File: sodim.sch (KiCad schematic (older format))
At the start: 4 parts

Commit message: Update edge connector
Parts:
- J? (x2): footprint lpddr4-testbed-footprints:SODIMM_DDR4_EDGE -> antmicro-footprints:SODIMM_DDR4_EDGE; symbol lpddr4-testbed:ddr4-sodimm-edge-connector -> antmicroMemoryConnectorsPCCardSockets:ddr4-sodimm-edge-connector
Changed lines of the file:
@@
 SODIMM Connector
 $Comp
-L lpddr4-testbed:ddr4-sodimm-edge-connector J?
+L antmicroMemoryConnectorsPCCardSockets:ddr4-sodimm-edge-connector J?
 U 2 1 5FF3EE7F
 P 10650 5525
@@
 F 0 "J?" H 10650 8992 50  0000 C CNN
 F 1 "ddr4-sodimm-edge-connector" H 10650 8901 50  0000 C CNN
-F 2 "lpddr4-testbed-footprints:SODIMM_DDR4_EDGE" H 10350 1925 50  0001 L BNN
+F 2 "antmicro-footprints:SODIMM_DDR4_EDGE" H 10350 1925 50  0001 L BNN
 F 3 "" H 11650 5625 50  0001 L BNN
 	2    10650 5525
@@
 $EndComp
 $Comp
-L lpddr4-testbed:ddr4-sodimm-edge-connector J?
+L antmicroMemoryConnectorsPCCardSockets:ddr4-sodimm-edge-connector J?
 U 1 1 5FF3EE85
 P 6525 5800
@@
 F 0 "J?" H 6525 9365 50  0000 C CNN
 F 1 "ddr4-sodimm-edge-connector" H 6525 9274 50  0000 C CNN
-F 2 "lpddr4-testbed-footprints:SODIMM_DDR4_EDGE" H 6225 2200 50  0001 L BNN
+F 2 "antmicro-footprints:SODIMM_DDR4_EDGE" H 6225 2200 50  0001 L BNN
 F 3 "" H 7525 5900 50  0001 L BNN
 	1    6525 5800

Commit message: Connect power supplies and CHANNEL A signals to edge connector
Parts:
- removed C?: C_100n_0402_6V3, lpddr4-testbed-footprints:0402-cap, symbol lpddr4-testbed:C_100n_0402_6V3
- removed J? (x2): ddr4-sodimm-edge-connector, antmicro-footprints:SODIMM_DDR4_EDGE, symbol antmicroMemoryConnectorsPCCardSockets:ddr4-sodimm-edge-connector
- removed R?: R_40R2_0402, lpddr4-testbed-footprints:0402-res, symbol lpddr4-testbed:R_40R2_0402
- added J1: ddr4-sodimm-edge-connector, antmicro-footprints:SODIMM_DDR4_EDGE, symbol antmicroMemoryConnectorsPCCardSockets:ddr4-sodimm-edge-connector
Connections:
- net labels added: CA_0A, CA_1A, CKE0_A, CK_CA, CK_TA, CS0_A, DMI_0A, DMI_1A, DQ00_A, DQ01_A, DQ02_A, DQ03_A, DQ04_A, DQ05_A, DQ06_A, DQ07_A, DQ08_A, DQ09_A, DQ10_A, DQ11_A, DQ12_A, DQ13_A, DQ14_A, DQ15_A, DQ_S0_CA, DQ_S0_TA, DQ_S1_CA, DQ_S1_TA, VDD1, VDD2, VDDQ
- net labels removed: ACT_N, ALERT_N, BA0, BA1, BG0, BG1, CA0_A, CA0_B, CA1_A, CA1_B, CA2_B, CA3_B, CA4_B, CA5_B, CK0_C, CK0_T, CK1_C, CK1_T, CKE_0, CKE_1, CS0_N, CS_1_N, DDRVCC, DM0_N, DM1_N, DM2_N, DM3_N, DQ00, DQ01, DQ02, DQ03, DQ04, DQ05, DQ06, DQ07, DQ08, DQ09, DQ10, DQ11, DQ12, DQ13, DQ14, DQ15, DQ16, DQ17, DQ18, DQ19, DQ20, DQ21, DQ22, DQ23, DQ24, DQ25, DQ26, DQ27, DQ28, DQ29, DQ30, DQ31, DQS0_C, DQS0_T, DQS1_C, DQS1_T, DQS2_C, DQS2_T, DQS3_C, DQS3_T, EVENT_N, ODT0, ODT1, PARITY, RESET_CONN_N, SA0, SA1, SCL, SDA, VDDSPD, VPP, VREFCA, VTT
- wire segments 321 -> 214
- no-connect marks 65 -> 0
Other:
- note added: "1V1_SYS"
- note added: "1V8_SYS"
- note added: "VDDQ"
- note removed: "Bank adress"
- note removed: "Bank group\n"
- note removed: "Second LPDDR4 die"
- note removed: "Single LPDDR4 die"
- note removed: "What is taht pin?"

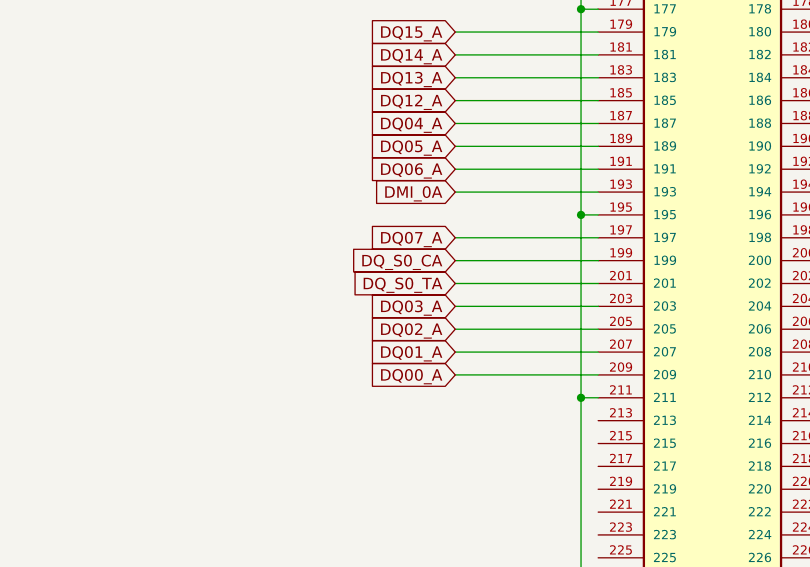
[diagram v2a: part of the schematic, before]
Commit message: Reverse connections of DQ4_A ... DQ0_A
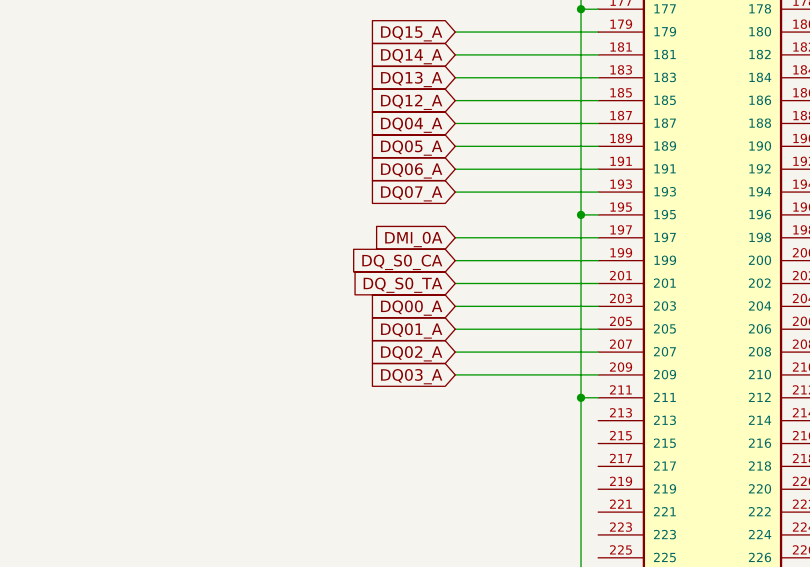
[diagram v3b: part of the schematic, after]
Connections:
- net DMI_0A: now also J1.197; no longer J1.193
- net DQ00_A: now also J1.203; no longer J1.209
- net DQ01_A: now also J1.205; no longer J1.207
- net DQ02_A: now also J1.207; no longer J1.205
- net DQ03_A: now also J1.209; no longer J1.203
- net DQ07_A: now also J1.193; no longer J1.197
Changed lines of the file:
@@
 Wire Wire Line
 	9500 5700 8875 5700
+Text GLabel 8875 5900 0    50   Input ~ 0
+DMI_0A
+Wire Wire Line
+	9500 5900 8875 5900
 Text GLabel 8875 5700 0    50   Input ~ 0
-DMI_0A
-Wire Wire Line
-	9500 5900 8875 5900
-Text GLabel 8875 5900 0    50   Input ~ 0
 DQ07_A
 Wire Wire Line
@@
 Wire Wire Line
 	9500 6200 8875 6200
+Text GLabel 8875 6500 0    50   Input ~ 0
+DQ03_A
+Wire Wire Line
+	9500 6300 8875 6300
+Text GLabel 8875 6400 0    50   Input ~ 0
+DQ02_A
+Wire Wire Line
+	9500 6400 8875 6400
+Text GLabel 8875 6300 0    50   Input ~ 0
+DQ01_A
+Wire Wire Line
+	9500 6500 8875 6500
 Text GLabel 8875 6200 0    50   Input ~ 0
-DQ03_A
-Wire Wire Line
-	9500 6300 8875 6300
-Text GLabel 8875 6300 0    50   Input ~ 0
-DQ02_A
-Wire Wire Line
-	9500 6400 8875 6400
-Text GLabel 8875 6400 0    50   Input ~ 0
-DQ01_A
-Wire Wire Line
-	9500 6500 8875 6500
-Text GLabel 8875 6500 0    50   Input ~ 0
 DQ00_A
 Wire Wire Line
@@
 	5725 2500 5850 2500
 $Comp
-L lpddr4-testbed:GND #PWR?
+L lpddr4-testbed:GND #PWR0101
 U 1 1 600CF473
 P 5850 9125
-F 0 "#PWR?" H 5850 8875 50  0001 C CNN
+F 0 "#PWR0101" H 5850 8875 50  0001 C CNN
 F 1 "GND" H 5855 8952 50  0000 C CNN
 F 2 "" H 5850 9125 50  0001 C CNN
@@
 $EndComp
 $Comp
-L lpddr4-testbed:GND #PWR?
+L lpddr4-testbed:GND #PWR0102
 U 1 1 600CF7AC
 P 9425 9125
-F 0 "#PWR?" H 9425 8875 50  0001 C CNN
+F 0 "#PWR0102" H 9425 8875 50  0001 C CNN
 F 1 "GND" H 9430 8952 50  0000 C CNN
 F 2 "" H 9425 9125 50  0001 C CNN
@@
 	4600 2500 4600 2600
 $Comp
-L lpddr4-testbed:GND #PWR?
+L lpddr4-testbed:GND #PWR0103
 U 1 1 600F8128
 P 4600 9125
-F 0 "#PWR?" H 4600 8875 50  0001 C CNN
+F 0 "#PWR0103" H 4600 8875 50  0001 C CNN
 F 1 "GND" H 4605 8952 50  0000 C CNN
 F 2 "" H 4600 9125 50  0001 C CNN
@@
 	10550 3700 10550 4400
 $Comp
-L lpddr4-testbed:GND #PWR?
+L lpddr4-testbed:GND #PWR0104
 U 1 1 6032AE1D
 P 10550 9125
-F 0 "#PWR?" H 10550 8875 50  0001 C CNN
+F 0 "#PWR0104" H 10550 8875 50  0001 C CNN
 F 1 "GND" H 10555 8952 50  0000 C CNN
 F 2 "" H 10550 9125 50  0001 C CNN

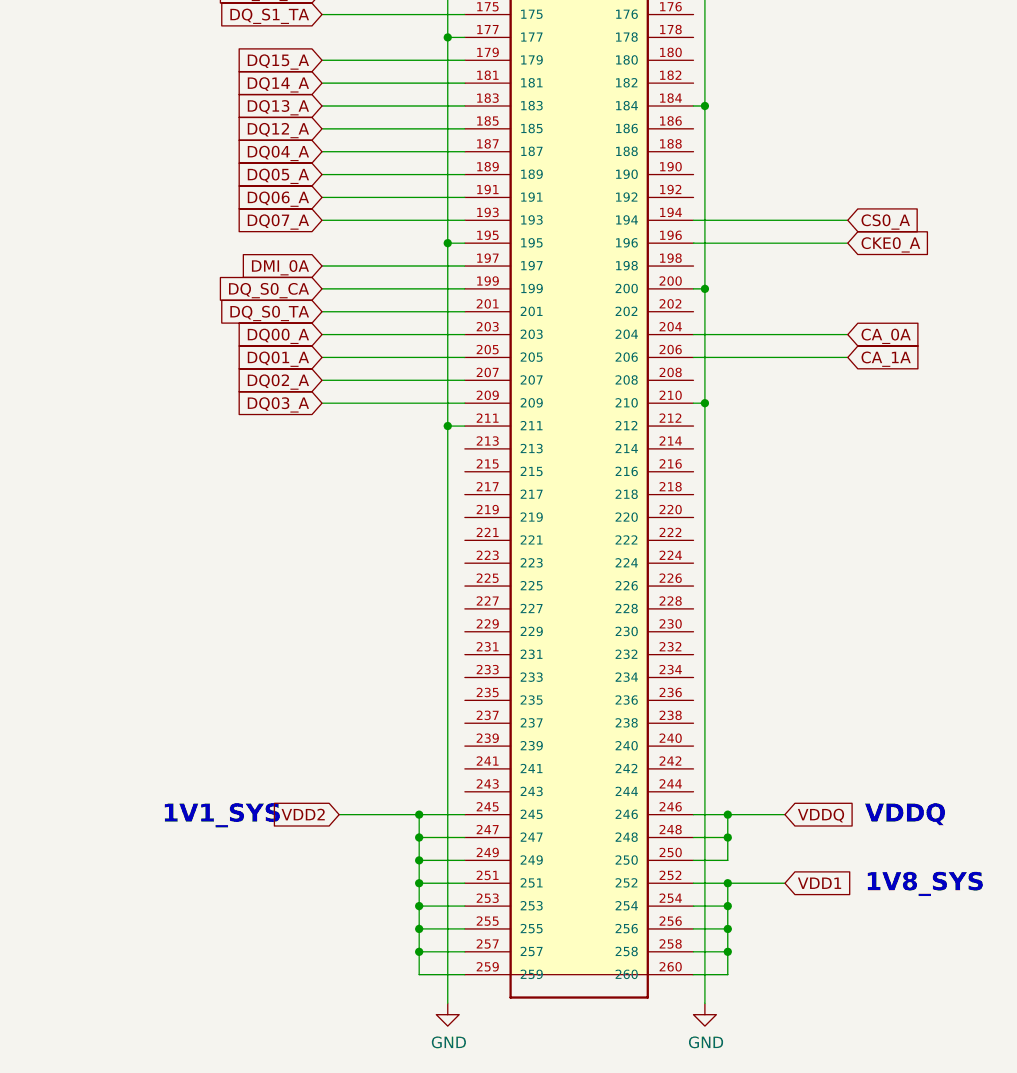
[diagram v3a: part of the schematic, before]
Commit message: Fully routed, DRC clean
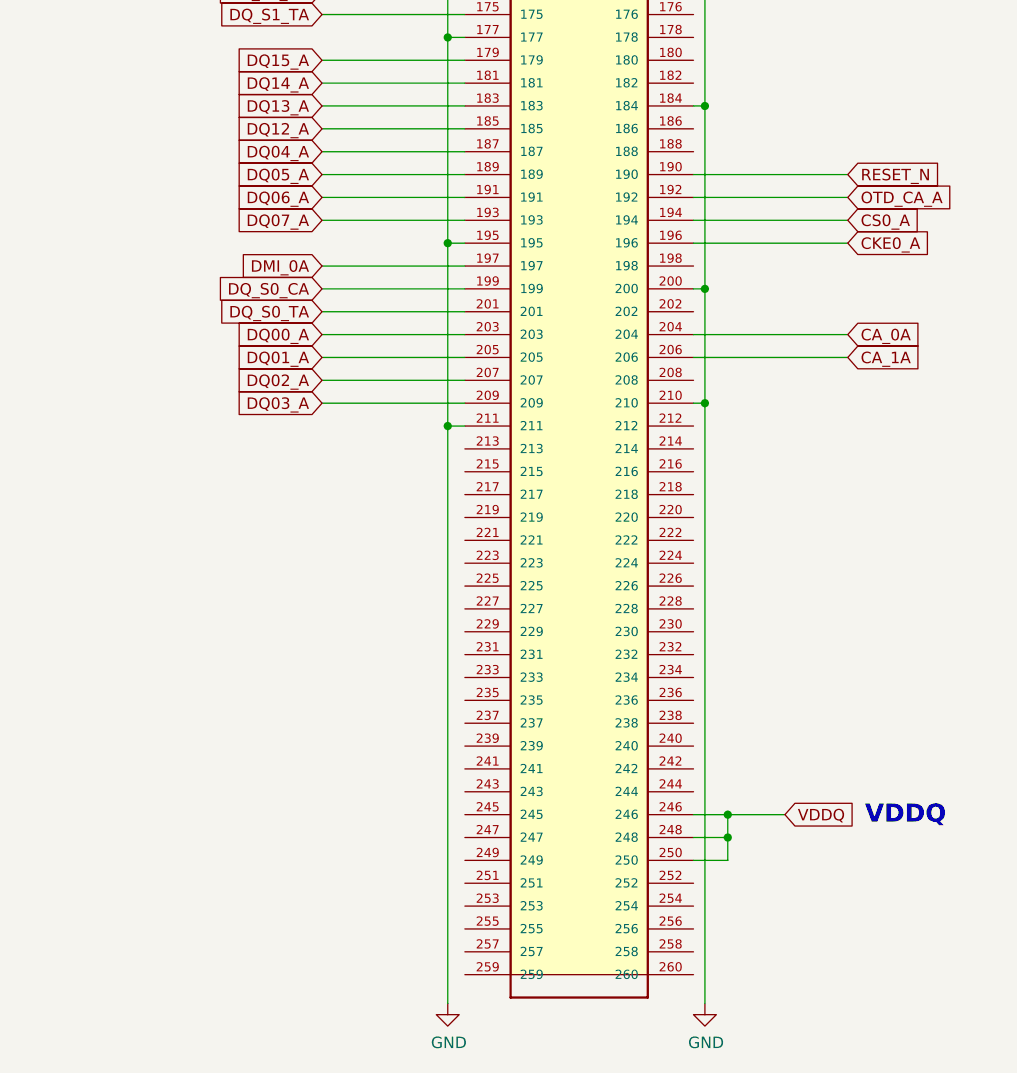
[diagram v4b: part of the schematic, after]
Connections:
- net VDD1: no longer J1.252, J1.254, J1.256, J1.258, J1.260
- net VDD2: no longer J1.245, J1.247, J1.249, J1.251, J1.253, J1.255, J1.257, J1.259
- net RESET_N: now reaches J1.190
- net OTD_CA_A: now reaches J1.192
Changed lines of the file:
@@
 $Descr A3 16535 11693
 encoding utf-8
-Sheet 3 4
+Sheet 2 3
 Title ""
 Date ""
@@
 U 1 1 600AC6A9
 P 5225 5800
+AR Path="/5FDC4A05/600AC6A9" Ref="J1"  Part="1"
+AR Path="/5FF943AC/600AC6A9" Ref="J?"  Part="1"
 F 0 "J1" H 5225 9365 50  0000 C CNN
 F 1 "ddr4-sodimm-edge-connector" H 5225 9274 50  0000 C CNN
@@
 U 2 1 600B3548
 P 10000 5800
+AR Path="/5FDC4A05/600B3548" Ref="J1"  Part="2"
+AR Path="/5FF943AC/600B3548" Ref="J?"  Part="2"
 F 0 "J1" H 10000 9365 50  0000 C CNN
 F 1 "ddr4-sodimm-edge-connector" H 10000 9274 50  0000 C CNN
@@
 U 1 1 600CF473
 P 5850 9125
+AR Path="/5FDC4A05/600CF473" Ref="#PWR0101"  Part="1"
+AR Path="/5FF943AC/600CF473" Ref="#PWR?"  Part="1"
 F 0 "#PWR0101" H 5850 8875 50  0001 C CNN
 F 1 "GND" H 5855 8952 50  0000 C CNN
@@
 	1    0    0    -1
 $EndComp
-$Comp
-L lpddr4-testbed:GND #PWR0102
-U 1 1 600CF7AC
-P 9425 9125
-F 0 "#PWR0102" H 9425 8875 50  0001 C CNN
-F 1 "GND" H 9430 8952 50  0000 C CNN
-F 2 "" H 9425 9125 50  0001 C CNN
-F 3 "" H 9425 9125 50  0001 C CNN
-	1    9425 9125
-	1    0    0    -1
-$EndComp
 Wire Wire Line
 	5725 4900 5850 4900
@@
 U 1 1 600F8128
 P 4600 9125
+AR Path="/5FDC4A05/600F8128" Ref="#PWR0103"  Part="1"
+AR Path="/5FF943AC/600F8128" Ref="#PWR?"  Part="1"
 F 0 "#PWR0103" H 4600 8875 50  0001 C CNN
 F 1 "GND" H 4605 8952 50  0000 C CNN
@@
 Text Notes 6500 8750 0    79   ~ 16
 VDDQ
-Wire Wire Line
-	10500 8600 10650 8600
-Wire Wire Line
-	10500 8700 10650 8700
-Wire Wire Line
-	10650 8700 10650 8600
-Connection ~ 10650 8600
-Wire Wire Line
-	10650 8600 10900 8600
-Wire Wire Line
-	10500 8800 10650 8800
-Wire Wire Line
-	10650 8800 10650 8700
-Connection ~ 10650 8700
-Wire Wire Line
-	10500 8900 10650 8900
-Wire Wire Line
-	10650 8900 10650 8800
-Connection ~ 10650 8800
-Wire Wire Line
-	10500 9000 10650 9000
-Wire Wire Line
-	10650 9000 10650 8900
-Connection ~ 10650 8900
 Text Notes 11250 8350 0    79   ~ 16
 VDDQ
-Text GLabel 10900 8600 2    50   Input ~ 0
-VDD1
-Text Notes 11250 8650 0    79   ~ 16
-1V8_SYS
-Wire Wire Line
-	9500 8300 9300 8300
-Wire Wire Line
-	9500 8400 9300 8400
-Wire Wire Line
-	9300 8400 9300 8300
-Connection ~ 9300 8300
-Wire Wire Line
-	9300 8300 8950 8300
-Wire Wire Line
-	9500 8500 9300 8500
-Wire Wire Line
-	9300 8500 9300 8400
-Connection ~ 9300 8400
-Wire Wire Line
-	9500 8600 9300 8600
-Wire Wire Line
-	9300 8600 9300 8500
-Connection ~ 9300 8500
-Wire Wire Line
-	9500 8700 9300 8700
-Wire Wire Line
-	9300 8700 9300 8600
-Connection ~ 9300 8600
-Wire Wire Line
-	9500 8800 9300 8800
-Wire Wire Line
-	9300 8800 9300 8700
-Connection ~ 9300 8700
-Wire Wire Line
-	9500 8900 9300 8900
-Wire Wire Line
-	9300 8900 9300 8800
-Connection ~ 9300 8800
-Wire Wire Line
-	9500 9000 9300 9000
-Wire Wire Line
-	9300 9000 9300 8900
-Connection ~ 9300 8900
-Text Notes 8175 8350 0    79   ~ 16
-1V1_SYS
-Text GLabel 8950 8300 0    50   Input ~ 0
-VDD2
 Wire Wire Line
 	10500 8300 10650 8300
@@
 U 1 1 6032AE1D
 P 10550 9125
+AR Path="/5FDC4A05/6032AE1D" Ref="#PWR0104"  Part="1"
+AR Path="/5FF943AC/6032AE1D" Ref="#PWR?"  Part="1"
 F 0 "#PWR0104" H 10550 8875 50  0001 C CNN
 F 1 "GND" H 10555 8952 50  0000 C CNN
@@
 Wire Wire Line
 	10500 5700 11175 5700
-Text GLabel 11175 5800 2    50   Input ~ 0
-CKE0_A
-Wire Wire Line
-	10500 5800 11175 5800
 Text GLabel 11175 6200 2    50   Input ~ 0
 CA_0A
@@
 Wire Wire Line
 	10550 5200 10550 6000
+Wire Wire Line
+	10500 5600 11175 5600
+Text GLabel 11175 5600 2    50   Input ~ 0
+OTD_CA_A
+Wire Wire Line
+	10500 5500 11175 5500
+Text GLabel 11175 5500 2    50   Input ~ 0
+RESET_N
+Wire Wire Line
+	10500 5800 11175 5800
+Text GLabel 11175 5800 2    50   Input ~ 0
+CKE0_A
+$Comp
+L lpddr4-testbed:GND #PWR?
+U 1 1 6015ECEA
+P 9425 9125
+AR Path="/5FDC4A05/6015ECEA" Ref="#PWR?"  Part="1"
+AR Path="/5FF943AC/6015ECEA" Ref="#PWR?"  Part="1"
+F 0 "#PWR?" H 9425 8875 50  0001 C CNN
+F 1 "GND" H 9430 8952 50  0000 C CNN
+F 2 "" H 9425 9125 50  0001 C CNN
+F 3 "" H 9425 9125 50  0001 C CNN
+	1    9425 9125
+	1    0    0    -1
+$EndComp
 $EndSCHEMATC

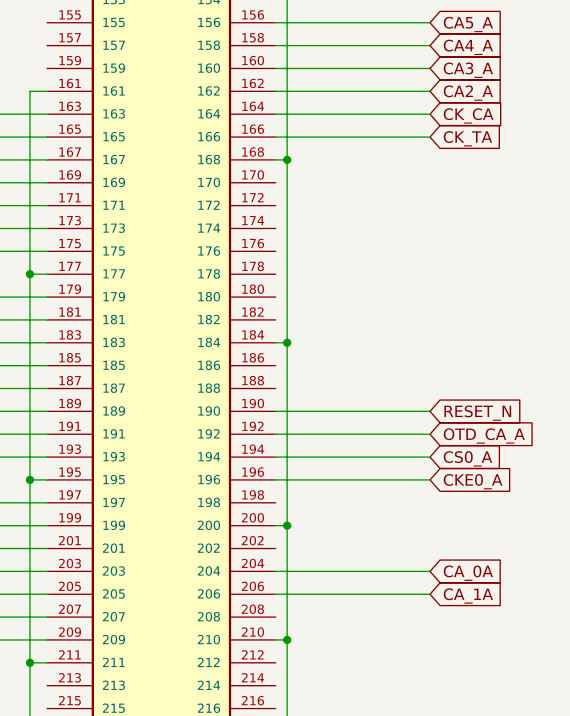
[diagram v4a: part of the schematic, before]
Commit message: Reconnect RESET_N and ODT_CA to IO_P4 and IO_N5
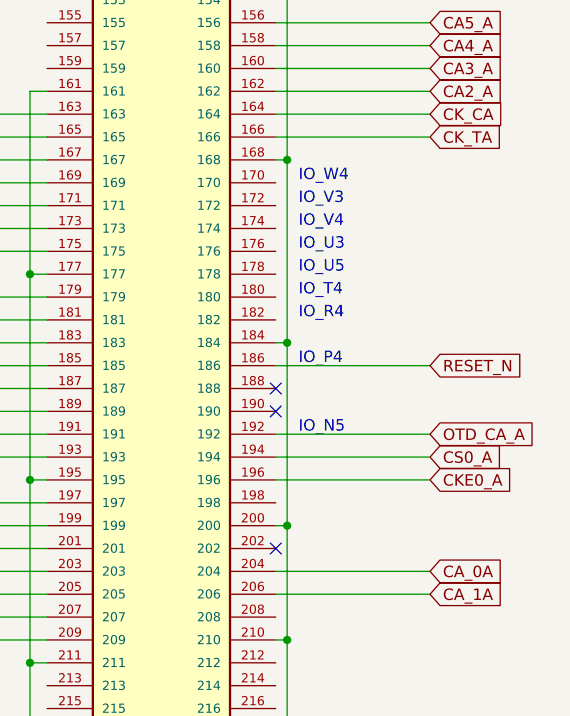
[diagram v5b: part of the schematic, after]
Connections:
- net RESET_N: now also J1.186; no longer J1.190
- no-connect marks 0 -> 3
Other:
- note added: "IO_N5"
- note added: "IO_P4"
- note added: "IO_R4"
- note added: "IO_T4"
- note added: "IO_U3"
- note added: "IO_U5"
- note added: "IO_V3"
- note added: "IO_V4"
- note added: "IO_W4"
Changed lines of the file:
@@
 Text GLabel 11175 5600 2    50   Input ~ 0
 OTD_CA_A
-Wire Wire Line
-	10500 5500 11175 5500
-Text GLabel 11175 5500 2    50   Input ~ 0
+Text GLabel 11175 5300 2    50   Input ~ 0
 RESET_N
 Wire Wire Line
@@
 CKE0_A
 $Comp
-L lpddr4-testbed:GND #PWR?
+L lpddr4-testbed:GND #PWR0102
 U 1 1 6015ECEA
 P 9425 9125
-AR Path="/5FDC4A05/6015ECEA" Ref="#PWR?"  Part="1"
+AR Path="/5FDC4A05/6015ECEA" Ref="#PWR0102"  Part="1"
 AR Path="/5FF943AC/6015ECEA" Ref="#PWR?"  Part="1"
-F 0 "#PWR?" H 9425 8875 50  0001 C CNN
+F 0 "#PWR0102" H 9425 8875 50  0001 C CNN
 F 1 "GND" H 9430 8952 50  0000 C CNN
 F 2 "" H 9425 9125 50  0001 C CNN
@@
 	1    0    0    -1
 $EndComp
+Text Notes 10600 5300 0    50   ~ 0
+IO_P4
+Text Notes 10600 5100 0    50   ~ 0
+IO_R4
+Text Notes 10600 5000 0    50   ~ 0
+IO_T4
+Text Notes 10600 4900 0    50   ~ 0
+IO_U5
+Text Notes 10600 4800 0    50   ~ 0
+IO_U3
+Text Notes 10600 4700 0    50   ~ 0
+IO_V4
+Text Notes 10600 4600 0    50   ~ 0
+IO_V3
+Text Notes 10600 4500 0    50   ~ 0
+IO_W4
+Wire Wire Line
+	10500 5300 11175 5300
+NoConn ~ 10500 5400
+NoConn ~ 10500 5500
+Text Notes 10600 5600 0    50   ~ 0
+IO_N5
+NoConn ~ 10500 6100
 $EndSCHEMATC

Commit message: Update local libs, resolve DRC
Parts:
- J1: footprint antmicro-footprints:SODIMM_DDR4_EDGE -> lpddr4-testbed-footprints:SODIMM_DDR4_EDGE; symbol antmicroMemoryConnectorsPCCardSockets:ddr4-sodimm-edge-connector -> lpddr4-testbed:ddr4-sodimm-edge-connector
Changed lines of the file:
@@
 SODIMM Connector
 $Comp
-L antmicroMemoryConnectorsPCCardSockets:ddr4-sodimm-edge-connector J1
+L lpddr4-testbed:ddr4-sodimm-edge-connector J1
 U 1 1 600AC6A9
 P 5225 5800
@@
 F 0 "J1" H 5225 9365 50  0000 C CNN
 F 1 "ddr4-sodimm-edge-connector" H 5225 9274 50  0000 C CNN
-F 2 "antmicro-footprints:SODIMM_DDR4_EDGE" H 4925 2400 50  0001 L BNN
+F 2 "lpddr4-testbed-footprints:SODIMM_DDR4_EDGE" H 4925 2400 50  0001 L BNN
 F 3 "" H 6225 5900 50  0001 L BNN
 	1    5225 5800
@@
 $EndComp
 $Comp
-L antmicroMemoryConnectorsPCCardSockets:ddr4-sodimm-edge-connector J1
+L lpddr4-testbed:ddr4-sodimm-edge-connector J1
 U 2 1 600B3548
 P 10000 5800
@@
 F 0 "J1" H 10000 9365 50  0000 C CNN
 F 1 "ddr4-sodimm-edge-connector" H 10000 9274 50  0000 C CNN
-F 2 "antmicro-footprints:SODIMM_DDR4_EDGE" H 9700 2400 50  0001 L BNN
+F 2 "lpddr4-testbed-footprints:SODIMM_DDR4_EDGE" H 9700 2400 50  0001 L BNN
 F 3 "" H 11000 5900 50  0001 L BNN
 	2    10000 5800

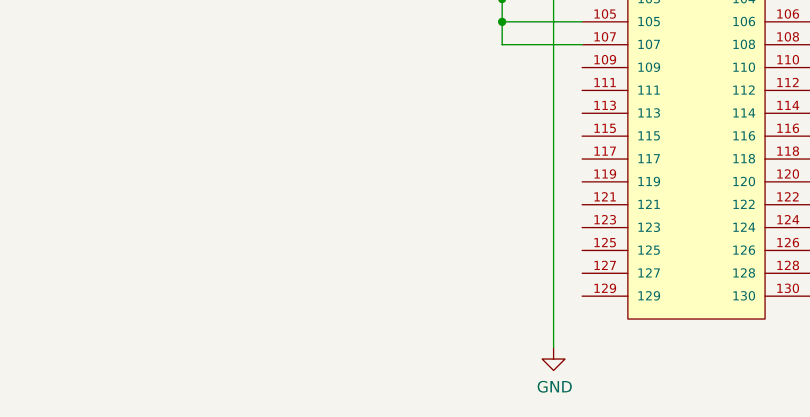
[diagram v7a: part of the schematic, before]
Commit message: Added sheet for EEPROM/LEDs
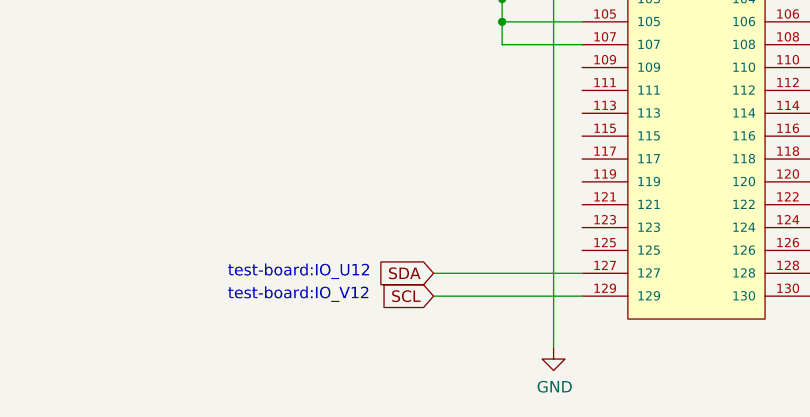
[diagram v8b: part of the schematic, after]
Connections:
- net SDA: now reaches J1.127
- net SCL: now reaches J1.129
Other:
- note added: "test-board:IO_U12"
- note added: "test-board:IO_V12"
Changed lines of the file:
@@
 $Descr A3 16535 11693
 encoding utf-8
-Sheet 2 3
+Sheet 2 4
 Title ""
 Date ""
@@
 IO_N5
 NoConn ~ 10500 6100
+Text GLabel 4075 8800 0    50   Input ~ 0
+SDA
+Text GLabel 4075 8900 0    50   Input ~ 0
+SCL
+Text Notes 3175 8825 0    50   ~ 0
+test-board:IO_U12
+Text Notes 3175 8925 0    50   ~ 0
+test-board:IO_V12
+Wire Wire Line
+	4075 8800 4725 8800
+Wire Wire Line
+	4075 8900 4725 8900
 $EndSCHEMATC
